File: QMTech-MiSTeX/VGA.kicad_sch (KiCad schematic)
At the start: 7 parts

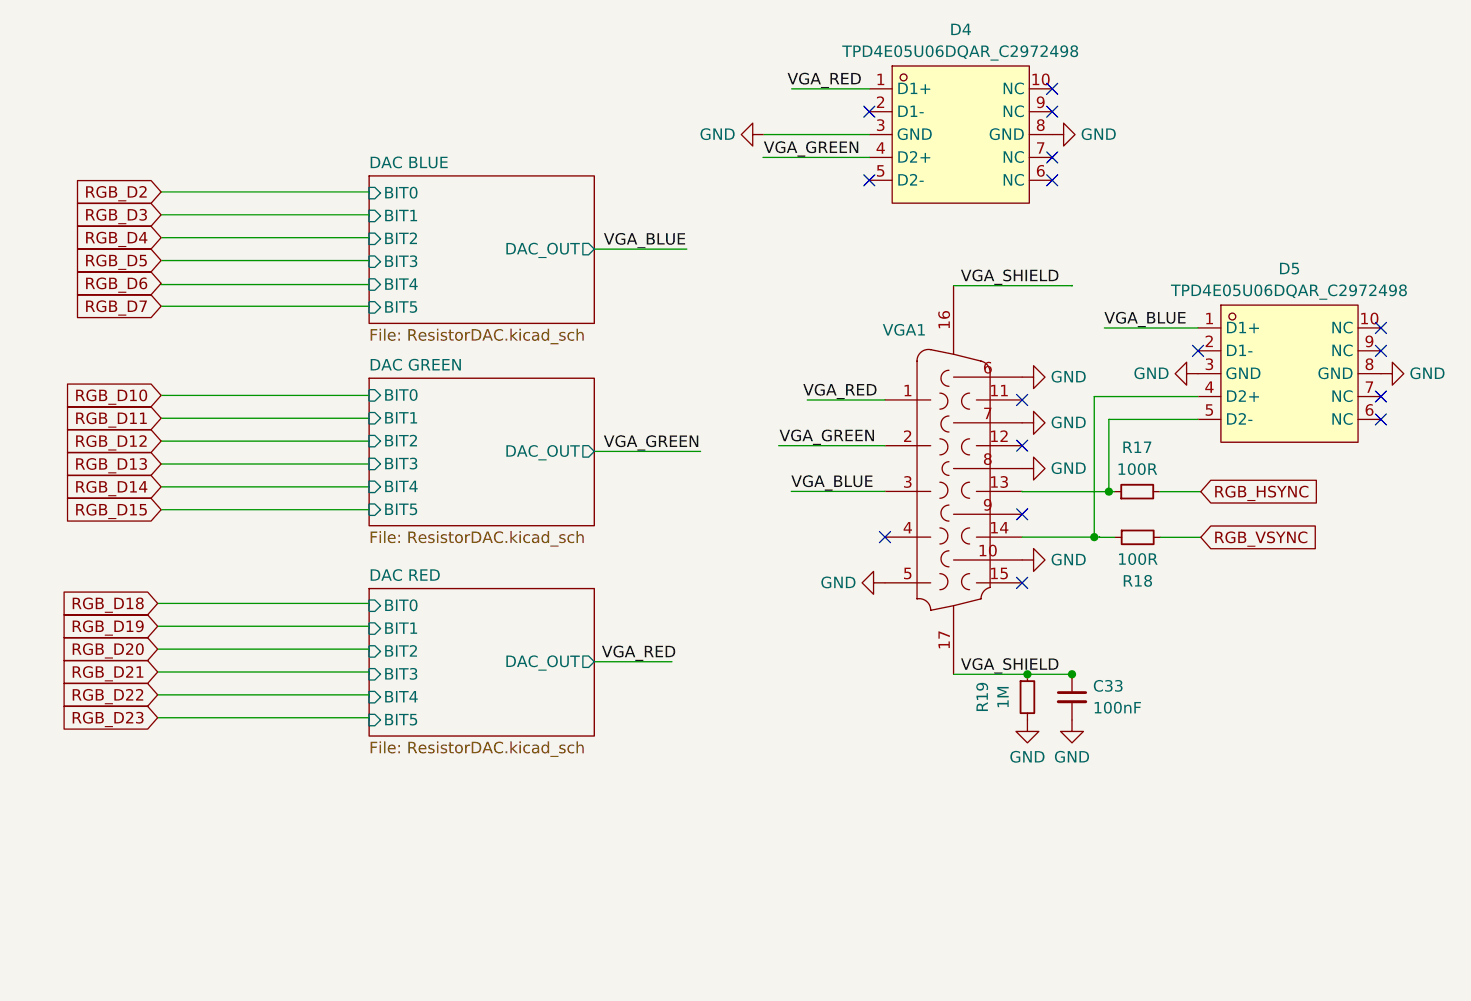
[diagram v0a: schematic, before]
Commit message: show the schematic borders and fix the design to fit
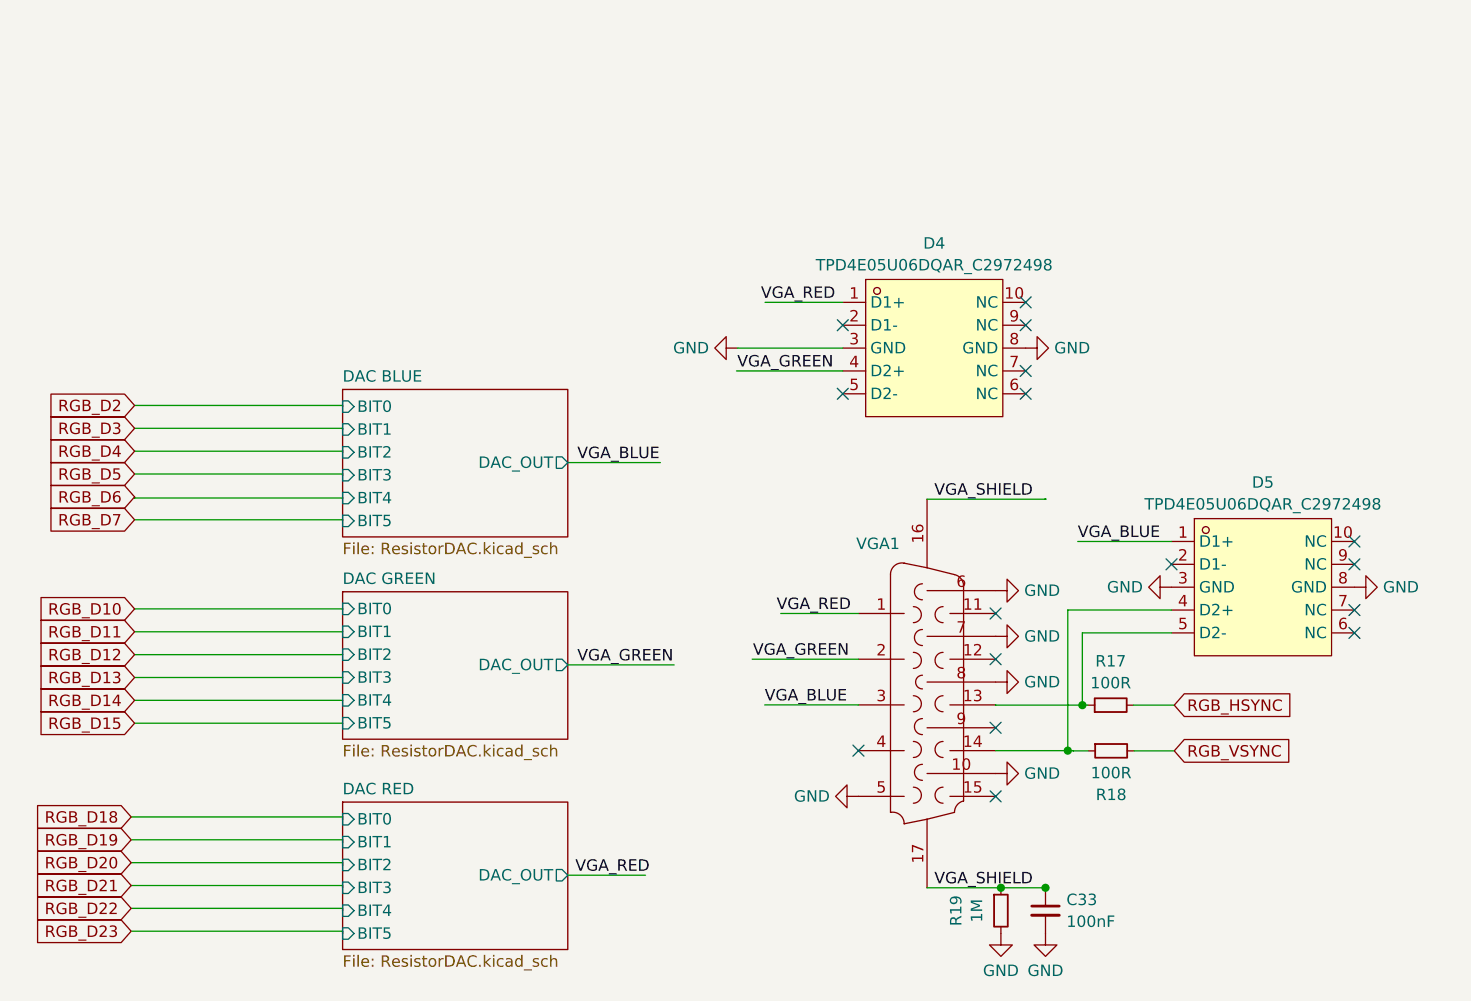
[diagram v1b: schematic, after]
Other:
- moved on the sheet: C33, D4, D5, R17, R18, R19, VGA1
